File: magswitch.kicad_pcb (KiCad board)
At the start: 2 copper layers, 14 x 18.2 mm, 13 parts, among them Q1 BSS138, Q2 Q_PMOS_GDS, U1 SM351LT, U2 S-812C33AMC-C2NT2U

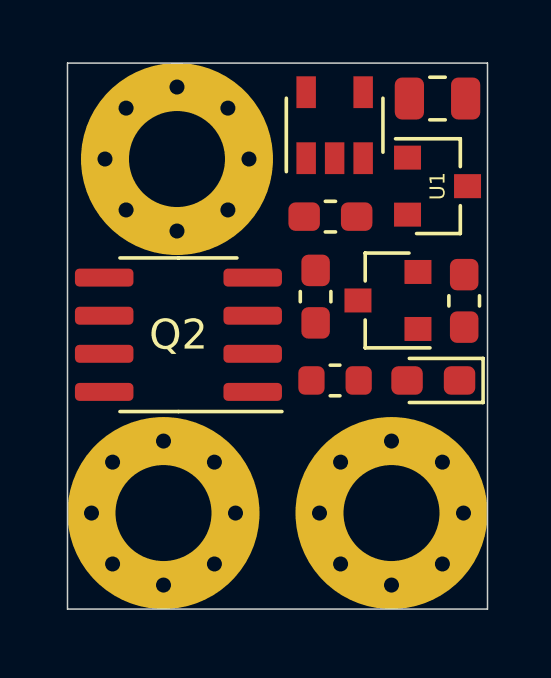
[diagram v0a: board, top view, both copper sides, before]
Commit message: Complete board tracing.
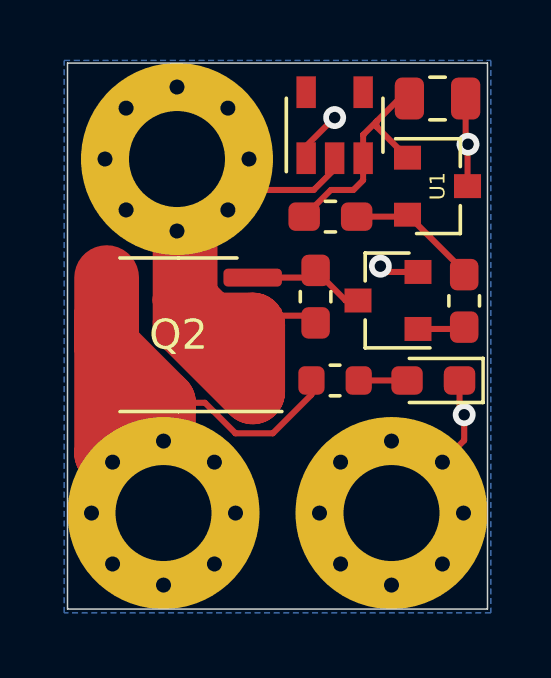
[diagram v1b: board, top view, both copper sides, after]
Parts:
- C1: value C -> 10uF
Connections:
- H1 pad 1: /Out -> /OUT
- R1 pad 1: /Out -> /OUT
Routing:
- net /IN: track 0.00 -> 23.1 mm
- net /OUT: track 0.00 -> 22.4 mm
- net GND: track 0.00 -> 11.5 mm, vias 0 -> 4
- net +3V3: track 0.00 -> 7.66 mm
- net Net-(R3-Pad2): track 0.00 -> 4.50 mm
- net Net-(Q1-Pad3): track 0.00 -> 4.02 mm
- net Net-(D1-Pad2): track 0.00 -> 1.61 mm
- net Net-(Q1-Pad1): track 0.00 -> 1.57 mm
- added copper zone on B.Cu, net GND

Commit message: Add pdf
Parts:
- added G***: LOGO, Team_Logo:Logo_SilkScreen_5mm, B.Cu at (3.43, -15.6)
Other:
- board text added: "GND"
- board text added: "IN"
- board text added: "Mag Switch Z. Mears 2021-04-10"
- board text added: "OUT"
